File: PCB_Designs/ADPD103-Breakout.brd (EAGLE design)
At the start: 100 x 80 mm, 3 parts

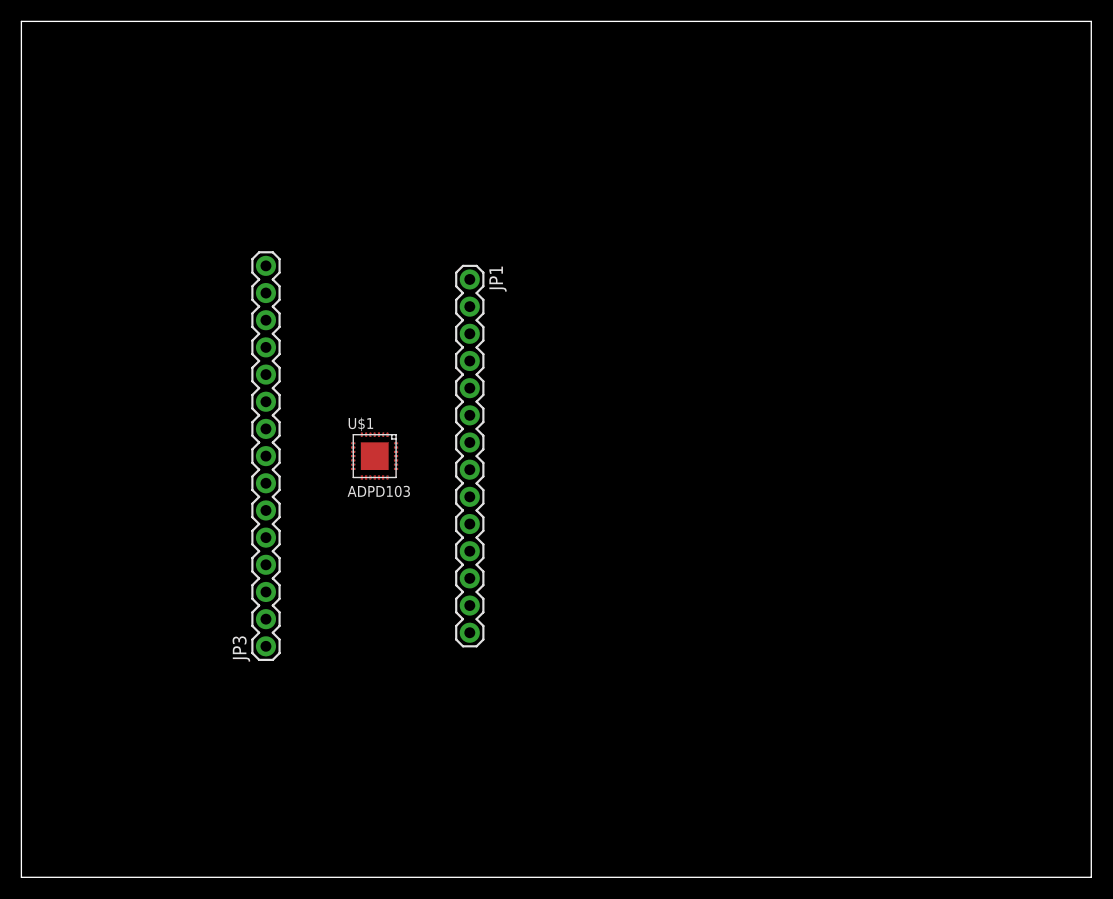
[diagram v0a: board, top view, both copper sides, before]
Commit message: first order sent to OSHPark
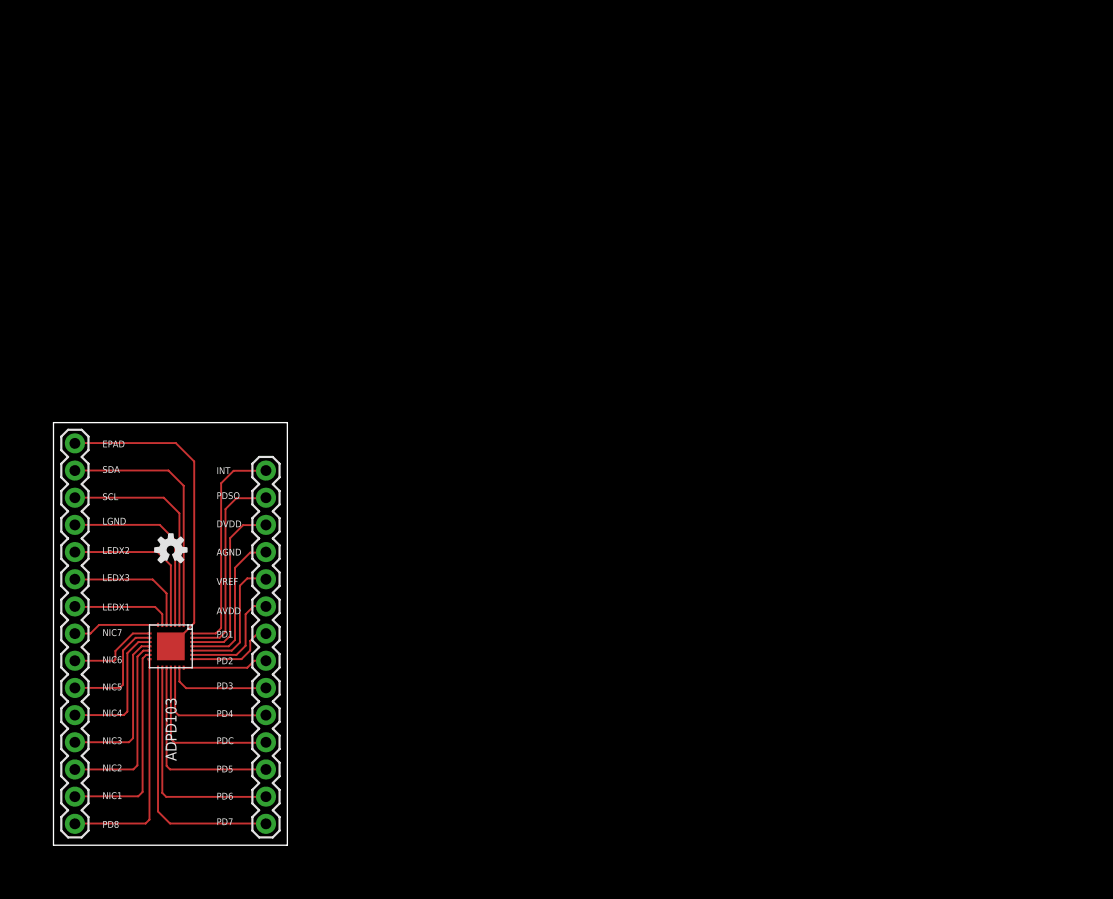
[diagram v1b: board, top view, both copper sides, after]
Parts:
- added LOGO1: OSHW-LOGOS, SparkFun-Aesthetics:OSHW-LOGO-S
- moved JP1 54.3 mm to (22.9, 5.00), turned to 90 degrees
- moved U$1 26.1 mm to (14.0, 21.6)
- moved JP3 24.4 mm to (5.00, 5.00)
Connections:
- net N$1: now also JP1.14; no longer JP1.1
- net N$10: now also JP1.5; no longer JP1.10
- net N$11: now also JP1.4; no longer JP1.11
- net N$12: now also JP1.3; no longer JP1.12
- net N$13: now also JP1.2; no longer JP1.13
- net N$14: now also JP1.1; no longer JP1.14
- net N$2: now also JP1.13; no longer JP1.2
- net N$3: now also JP1.12; no longer JP1.3
- net N$4: now also JP1.11; no longer JP1.4
- net N$5: now also JP1.10; no longer JP1.5
- net N$6: now also JP1.9; no longer JP1.6
- net N$7: now also JP1.8; no longer JP1.7
- net N$8: now also JP1.7; no longer JP1.8
- net N$9: now also JP1.6; no longer JP1.9
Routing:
- net N$23: track 0.00 -> 30.1 mm
- net N$14: track 0.00 -> 24.0 mm
- net N$24: track 0.00 -> 23.8 mm
- net N$15: track 0.00 -> 22.1 mm
- net N$13: track 0.00 -> 21.6 mm
- net N$1: track 0.00 -> 21.1 mm
- net N$25: track 0.00 -> 20.8 mm
- net N$16: track 0.00 -> 19.8 mm
- net N$2: track 0.00 -> 19.0 mm
- net N$12: track 0.00 -> 18.6 mm
- net N$26: track 0.00 -> 17.9 mm
- net N$17: track 0.00 -> 17.5 mm
- net N$3: track 0.00 -> 16.8 mm
- net N$11: track 0.00 -> 15.7 mm
- net N$18: track 0.00 -> 15.3 mm
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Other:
- board size 100 x 80 mm -> 21.9 x 39.5 mm
- board text added: "AGND"
- board text added: "AVDD"
- board text added: "DVDD"
- board text added: "EPAD"
- board text added: "INT"
- board text added: "LEDX1"
- board text added: "LEDX2"
- board text added: "LEDX3"
- board text added: "LGND"
- board text added: "NIC1"
- board text added: "NIC2"
- board text added: "NIC3"
- board text added: "NIC4"
- board text added: "NIC5"
- board text added: "NIC6"
- board text added: "NIC7"
- board text added: "Orlando S. Hoilett CalvaryEng, IICEPD ADPD103 Breakout"
- board text added: "PD1"
- board text added: "PD2"
- board text added: "PD3"
- board text added: "PD4"
- board text added: "PD5"
- board text added: "PD6"
- board text added: "PD7"
- board text added: "PD8"
- board text added: "PDC"
- board text added: "PDSO"
- board text added: "SCL"
- board text added: "SDA"
- board text added: "VREF"
